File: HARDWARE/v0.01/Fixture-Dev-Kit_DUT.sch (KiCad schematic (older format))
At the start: 31 parts, among them J5? CHIP4LH, J6? CHIP4RH, J8? CHIP4B2B

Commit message: editing some files. cleaning stuff up.
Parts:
- J?: value JST -> BAT
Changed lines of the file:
@@
 P 900 6150
 F 0 "J?" H 900 6250 50  0000 C CNN
-F 1 "JST" H 900 5950 50  0000 C CNN
+F 1 "BAT" H 900 5950 50  0000 C CNN
 F 2 "" H 900 6150 50  0001 C CNN
 F 3 "" H 900 6150 50  0001 C CNN

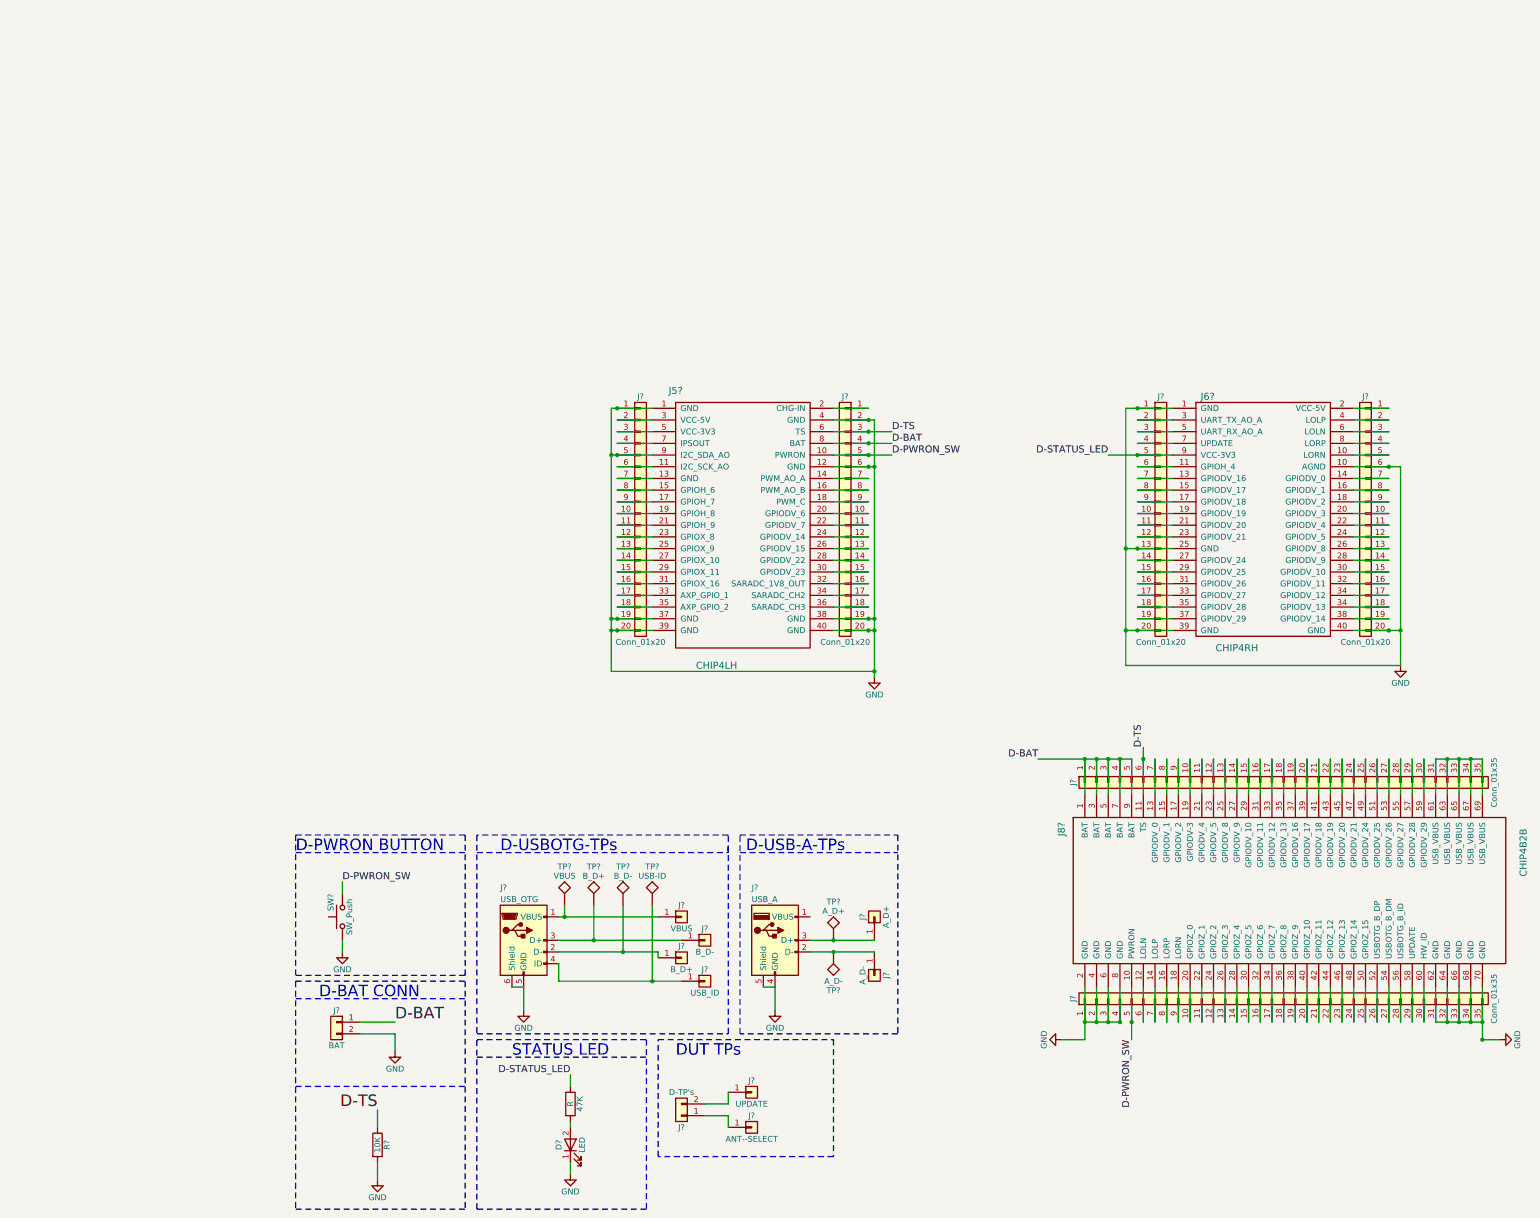
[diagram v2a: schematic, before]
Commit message: adding netlist and design rules check
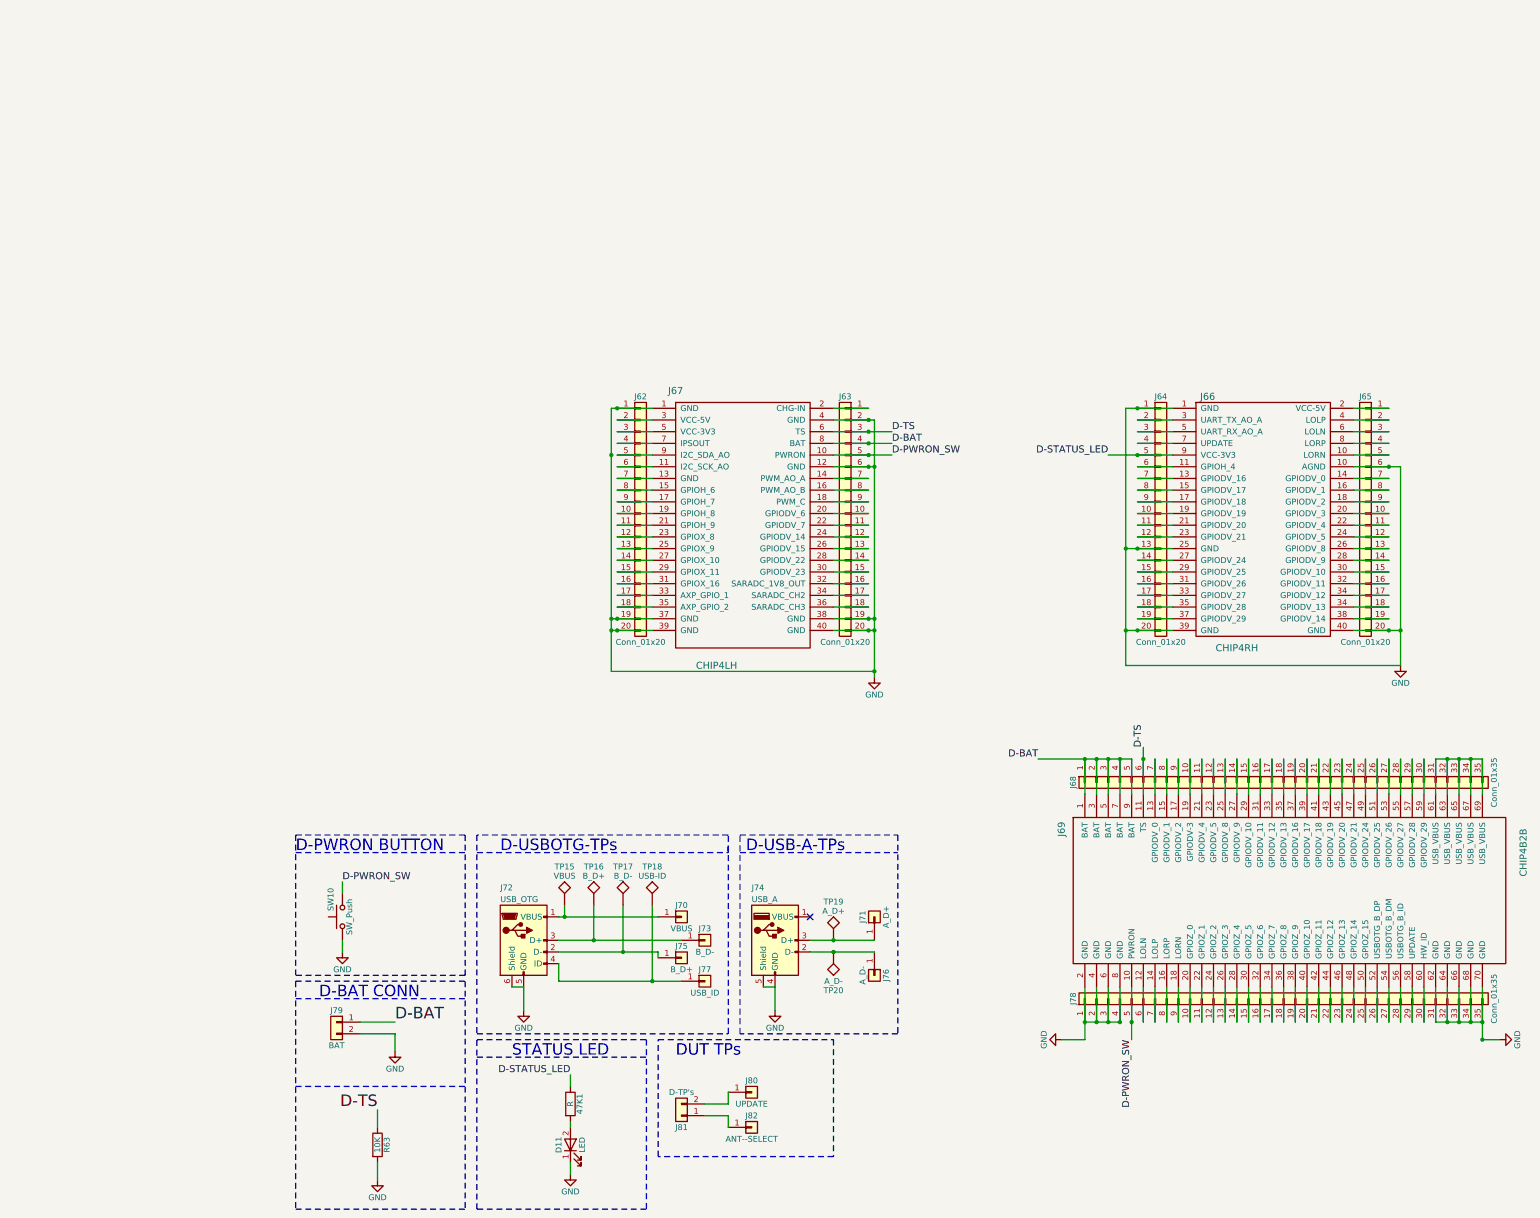
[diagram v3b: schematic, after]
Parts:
- gave numbers to parts that had none: 30
- renumbered 47K to 47K1
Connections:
- net GND: no longer J62.5 (Pin_5), J67.9 (I2C_SDA_AO)
- new net: J62.5 (Pin_5), J67.9 (I2C_SDA_AO)
- no-connect marks 0 -> 1
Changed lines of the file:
@@
 $EndDescr
 $Comp
-L Conn_01x20 J?
+L Conn_01x20 J65
 U 1 1 59EE26A0
 P 9700 1800
-F 0 "J?" H 9700 2800 50  0000 C CNN
+F 0 "J65" H 9700 2800 50  0000 C CNN
 F 1 "Conn_01x20" H 9700 700 50  0000 C CNN
 F 2 "" H 9700 1800 50  0001 C CNN
@@
 $EndComp
 $Comp
-L Conn_01x20 J?
+L Conn_01x20 J64
 U 1 1 59EE26E4
 P 7950 1800
-F 0 "J?" H 7950 2800 50  0000 C CNN
+F 0 "J64" H 7950 2800 50  0000 C CNN
 F 1 "Conn_01x20" H 7950 700 50  0000 C CNN
 F 2 "" H 7950 1800 50  0001 C CNN
@@
 $EndComp
 $Comp
-L Conn_01x20 J?
+L Conn_01x20 J63
 U 1 1 59EE2815
 P 5250 1800
-F 0 "J?" H 5250 2800 50  0000 C CNN
+F 0 "J63" H 5250 2800 50  0000 C CNN
 F 1 "Conn_01x20" H 5250 700 50  0000 C CNN
 F 2 "" H 5250 1800 50  0001 C CNN
@@
 $EndComp
 $Comp
-L Conn_01x20 J?
+L Conn_01x20 J62
 U 1 1 59EE289C
 P 3500 1800
-F 0 "J?" H 3500 2800 50  0000 C CNN
+F 0 "J62" H 3500 2800 50  0000 C CNN
 F 1 "Conn_01x20" H 3500 700 50  0000 C CNN
 F 2 "" H 3500 1800 50  0001 C CNN
@@
 	3600 1200 3300 1200
 Wire Wire Line
-	3250 1300 3600 1300
-Wire Wire Line
 	3600 1400 3300 1400
 Wire Wire Line
@@
 	5450 900  5150 900
 $Comp
-L GND #PWR?
+L GND #PWR059
 U 1 1 59EE39D0
 P 10000 3100
-F 0 "#PWR?" H 10000 2850 50  0001 C CNN
+F 0 "#PWR059" H 10000 2850 50  0001 C CNN
 F 1 "GND" H 10000 2950 50  0000 C CNN
 F 2 "" H 10000 3100 50  0001 C CNN
@@
 Connection ~ 7750 2800
 $Comp
-L GND #PWR?
+L GND #PWR060
 U 1 1 59EE3CBF
 P 5500 3200
-F 0 "#PWR?" H 5500 2950 50  0001 C CNN
+F 0 "#PWR060" H 5500 2950 50  0001 C CNN
 F 1 "GND" H 5500 3050 50  0000 C CNN
 F 2 "" H 5500 3200 50  0001 C CNN
@@
 Connection ~ 3300 2700
 Connection ~ 3250 1300
-Connection ~ 3300 1300
-$Comp
-L SW_Push SW?
+$Comp
+L SW_Push SW10
 U 1 1 59EE41F3
 P 950 5250
-F 0 "SW?" H 1000 5350 50  0000 L CNN
+F 0 "SW10" H 1000 5350 50  0000 L CNN
 F 1 "SW_Push" H 950 5190 50  0000 C CNN
 F 2 "" H 950 5450 50  0001 C CNN
@@
 D-PWRON_SW
 $Comp
-L GND #PWR?
+L GND #PWR061
 U 1 1 59EE44BA
 P 950 5550
-F 0 "#PWR?" H 950 5300 50  0001 C CNN
+F 0 "#PWR061" H 950 5300 50  0001 C CNN
 F 1 "GND" H 950 5400 50  0000 C CNN
 F 2 "" H 950 5550 50  0001 C CNN
@@
 D-BAT
 $Comp
-L Conn_01x02 J?
+L Conn_01x02 J79
 U 1 1 59EE490D
 P 900 6150
-F 0 "J?" H 900 6250 50  0000 C CNN
+F 0 "J79" H 900 6250 50  0000 C CNN
 F 1 "BAT" H 900 5950 50  0000 C CNN
 F 2 "" H 900 6150 50  0001 C CNN
@@
 $EndComp
 $Comp
-L GND #PWR?
+L GND #PWR062
 U 1 1 59EE4976
 P 1400 6400
-F 0 "#PWR?" H 1400 6150 50  0001 C CNN
+F 0 "#PWR062" H 1400 6150 50  0001 C CNN
 F 1 "GND" H 1400 6250 50  0000 C CNN
 F 2 "" H 1400 6400 50  0001 C CNN
@@
 D-BAT CONN\n
 $Comp
-L CHIP4B2B J8?
+L CHIP4B2B J69
 U 1 1 59EE53E4
 P 10800 5000
-F 0 "J8?" H 10300 8700 60  0000 C CNN
+F 0 "J69" H 10300 8700 60  0000 C CNN
 F 1 "CHIP4B2B" H 10500 4750 60  0000 C CNN
 F 2 "" H 10900 6550 60  0001 C CNN
@@
 $EndComp
 $Comp
-L Conn_01x35 J?
+L Conn_01x35 J78
 U 1 1 59EE5553
 P 9000 5950
-F 0 "J?" H 9000 7750 50  0000 C CNN
+F 0 "J78" H 9000 7750 50  0000 C CNN
 F 1 "Conn_01x35" H 9000 4150 50  0000 C CNN
 F 2 "" H 9000 5950 50  0001 C CNN
@@
 $EndComp
 $Comp
-L Conn_01x35 J?
+L Conn_01x35 J68
 U 1 1 59EE5A00
 P 9000 4100
-F 0 "J?" H 9000 5900 50  0000 C CNN
+F 0 "J68" H 9000 5900 50  0000 C CNN
 F 1 "Conn_01x35" H 9000 2300 50  0000 C CNN
 F 2 "" H 9000 4100 50  0001 C CNN
@@
 Connection ~ 10600 3900
 $Comp
-L GND #PWR?
+L GND #PWR063
 U 1 1 59EE8E82
 P 10850 6300
-F 0 "#PWR?" H 10850 6050 50  0001 C CNN
+F 0 "#PWR063" H 10850 6050 50  0001 C CNN
 F 1 "GND" H 10850 6150 50  0000 C CNN
 F 2 "" H 10850 6300 50  0001 C CNN
@@
 	10700 6300 10850 6300
 $Comp
-L GND #PWR?
+L GND #PWR064
 U 1 1 59EE9E75
 P 7100 6300
-F 0 "#PWR?" H 7100 6050 50  0001 C CNN
+F 0 "#PWR064" H 7100 6050 50  0001 C CNN
 F 1 "GND" H 7100 6150 50  0000 C CNN
 F 2 "" H 7100 6300 50  0001 C CNN
@@
 	1400 6250 1400 6400
 $Comp
-L GND #PWR?
+L GND #PWR065
 U 1 1 59EEAB1E
 P 1250 7500
-F 0 "#PWR?" H 1250 7250 50  0001 C CNN
+F 0 "#PWR065" H 1250 7250 50  0001 C CNN
 F 1 "GND" H 1250 7350 50  0000 C CNN
 F 2 "" H 1250 7500 50  0001 C CNN
@@
 $EndComp
 $Comp
-L R R?
+L R R63
 U 1 1 59EEAB48
 P 1250 7200
-F 0 "R?" V 1330 7200 50  0000 C CNN
+F 0 "R63" V 1330 7200 50  0000 C CNN
 F 1 "10K" V 1250 7200 50  0000 C CNN
 F 2 "" V 1180 7200 50  0001 C CNN
@@
 D-STATUS_LED
 $Comp
-L LED D?
+L LED D11
 U 1 1 59EEB9BD
 P 2900 7200
-F 0 "D?" H 2900 7300 50  0000 C CNN
+F 0 "D11" H 2900 7300 50  0000 C CNN
 F 1 "LED" H 2900 7100 50  0000 C CNN
 F 2 "" H 2900 7200 50  0001 C CNN
@@
 $EndComp
 $Comp
-L GND #PWR?
+L GND #PWR066
 U 1 1 59EEBA3C
 P 2900 7450
-F 0 "#PWR?" H 2900 7200 50  0001 C CNN
+F 0 "#PWR066" H 2900 7200 50  0001 C CNN
 F 1 "GND" H 2900 7300 50  0000 C CNN
 F 2 "" H 2900 7450 50  0001 C CNN
@@
 	2900 7450 2900 7350
 $Comp
-L R 47K
+L R 47K1
 U 1 1 59EEBC3E
 P 2900 6850
-F 0 "47K" V 2980 6850 50  0000 C CNN
+F 0 "47K1" V 2980 6850 50  0000 C CNN
 F 1 "R" V 2900 6850 50  0000 C CNN
 F 2 "" V 2830 6850 50  0001 C CNN
@@
 	2100 6450 3550 6450
 $Comp
-L CHIP4LH J5?
+L CHIP4LH J67
 U 1 1 59EF0A10
 P 4350 2950
-F 0 "J5?" H 3800 5150 60  0000 C CNN
+F 0 "J67" H 3800 5150 60  0000 C CNN
 F 1 "CHIP4LH" H 4150 2800 60  0000 C CNN
 F 2 "" H 4450 2950 60  0001 C CNN
@@
 $EndComp
 $Comp
-L CHIP4RH J6?
+L CHIP4RH J66
 U 1 1 59EF1105
 P 8850 2850
-F 0 "J6?" H 8350 4900 60  0000 C CNN
+F 0 "J66" H 8350 4900 60  0000 C CNN
 F 1 "CHIP4RH" H 8600 2750 60  0000 C CNN
 F 2 "" H 8900 2850 60  0001 C CNN
@@
 	7800 5850 7800 6150
 $Comp
-L USB_OTG J?
+L USB_OTG J72
 U 1 1 59EE3483
 P 2500 5450
-F 0 "J?" H 2300 5900 50  0000 L CNN
+F 0 "J72" H 2300 5900 50  0000 L CNN
 F 1 "USB_OTG" H 2300 5800 50  0000 L CNN
 F 2 "" H 2650 5400 50  0001 C CNN
@@
 $EndComp
 $Comp
-L Conn_01x01 J?
+L Conn_01x01 J70
 U 1 1 59EE3AA7
 P 3850 5250
-F 0 "J?" H 3850 5350 50  0000 C CNN
+F 0 "J70" H 3850 5350 50  0000 C CNN
 F 1 "VBUS" H 3850 5150 50  0000 C CNN
 F 2 "" H 3850 5250 50  0001 C CNN
@@
 $EndComp
 $Comp
-L Conn_01x01 J?
+L Conn_01x01 J73
 U 1 1 59EE3B2E
 P 4050 5450
-F 0 "J?" H 4050 5550 50  0000 C CNN
+F 0 "J73" H 4050 5550 50  0000 C CNN
 F 1 "B_D-" H 4050 5350 50  0000 C CNN
 F 2 "" H 4050 5450 50  0001 C CNN
@@
 $EndComp
 $Comp
-L Conn_01x01 J?
+L Conn_01x01 J75
 U 1 1 59EE3B75
 P 3850 5600
-F 0 "J?" H 3850 5700 50  0000 C CNN
+F 0 "J75" H 3850 5700 50  0000 C CNN
 F 1 "B_D+" H 3850 5500 50  0000 C CNN
 F 2 "" H 3850 5600 50  0001 C CNN
@@
 $EndComp
 $Comp
-L Conn_01x01 J?
+L Conn_01x01 J77
 U 1 1 59EE3BBF
 P 4050 5800
-F 0 "J?" H 4050 5900 50  0000 C CNN
+F 0 "J77" H 4050 5900 50  0000 C CNN
 F 1 "USB_ID" H 4050 5700 50  0000 C CNN
 F 2 "" H 4050 5800 50  0001 C CNN
@@
 $EndComp
 $Comp
-L TEST TP?
+L TEST TP15
 U 1 1 59EE3BFB
 P 2850 5150
-F 0 "TP?" H 2850 5450 50  0000 C BNN
+F 0 "TP15" H 2850 5450 50  0000 C BNN
 F 1 "VBUS" H 2850 5400 50  0000 C CNN
 F 2 "" H 2850 5150 50  0001 C CNN
@@
 $EndComp
 $Comp
-L TEST TP?
+L TEST TP16
 U 1 1 59EE3C66
 P 3100 5150
-F 0 "TP?" H 3100 5450 50  0000 C BNN
+F 0 "TP16" H 3100 5450 50  0000 C BNN
 F 1 "B_D+" H 3100 5400 50  0000 C CNN
 F 2 "" H 3100 5150 50  0001 C CNN
@@
 $EndComp
 $Comp
-L TEST TP?
+L TEST TP17
 U 1 1 59EE3CBB
 P 3350 5150
-F 0 "TP?" H 3350 5450 50  0000 C BNN
+F 0 "TP17" H 3350 5450 50  0000 C BNN
 F 1 "B_D-" H 3350 5400 50  0000 C CNN
 F 2 "" H 3350 5150 50  0001 C CNN
@@
 $EndComp
 $Comp
-L TEST TP?
+L TEST TP18
 U 1 1 59EE3D0F
 P 3600 5150
-F 0 "TP?" H 3600 5450 50  0000 C BNN
+F 0 "TP18" H 3600 5450 50  0000 C BNN
 F 1 "USB-ID" H 3600 5400 50  0000 C CNN
 F 2 "" H 3600 5150 50  0001 C CNN
@@
 	2800 5800 3850 5800
 $Comp
-L GND #PWR?
+L GND #PWR067
 U 1 1 59EE623C
 P 2500 6050
-F 0 "#PWR?" H 2500 5800 50  0001 C CNN
+F 0 "#PWR067" H 2500 5800 50  0001 C CNN
 F 1 "GND" H 2500 5900 50  0000 C CNN
 F 2 "" H 2500 6050 50  0001 C CNN
@@
 	4250 4700 4250 4650
 $Comp
-L USB_A J?
+L USB_A J74
 U 1 1 59EE80E3
 P 4650 5450
-F 0 "J?" H 4450 5900 50  0000 L CNN
+F 0 "J74" H 4450 5900 50  0000 L CNN
 F 1 "USB_A" H 4450 5800 50  0000 L CNN
 F 2 "" H 4800 5400 50  0001 C CNN
@@
 $EndComp
 $Comp
-L Conn_01x01 J?
+L Conn_01x01 J71
 U 1 1 59EE8606
 P 5500 5250
-F 0 "J?" H 5500 5350 50  0000 C CNN
+F 0 "J71" H 5500 5350 50  0000 C CNN
 F 1 "A_D+" H 5500 5150 50  0000 C CNN
 F 2 "" H 5500 5250 50  0001 C CNN
@@
 $EndComp
 $Comp
-L Conn_01x01 J?
+L Conn_01x01 J76
 U 1 1 59EE879F
 P 5500 5750
-F 0 "J?" H 5500 5850 50  0000 C CNN
+F 0 "J76" H 5500 5850 50  0000 C CNN
 F 1 "A_D-" H 5500 5650 50  0000 C CNN
 F 2 "" H 5500 5750 50  0001 C CNN
@@
 $EndComp
 $Comp
-L TEST TP?
+L TEST TP20
 U 1 1 59EE8980
 P 5150 5550
-F 0 "TP?" H 5150 5850 50  0000 C BNN
+F 0 "TP20" H 5150 5850 50  0000 C BNN
 F 1 "A_D-" H 5150 5800 50  0000 C CNN
 F 2 "" H 5150 5550 50  0001 C CNN
@@
 $EndComp
 $Comp
-L TEST TP?
+L TEST TP19
 U 1 1 59EE8A8A
 P 5150 5450
-F 0 "TP?" H 5150 5750 50  0000 C BNN
+F 0 "TP19" H 5150 5750 50  0000 C BNN
 F 1 "A_D+" H 5150 5700 50  0000 C CNN
 F 2 "" H 5150 5450 50  0001 C CNN
@@
 Connection ~ 5150 5550
 $Comp
-L GND #PWR?
+L GND #PWR068
 U 1 1 59EE91D1
 P 4650 6050
-F 0 "#PWR?" H 4650 5800 50  0001 C CNN
+F 0 "#PWR068" H 4650 5800 50  0001 C CNN
 F 1 "GND" H 4650 5900 50  0000 C CNN
 F 2 "" H 4650 6050 50  0001 C CNN
@@
 	4350 4700 5700 4700
 $Comp
-L Conn_01x01 J?
+L Conn_01x01 J80
 U 1 1 59EEA0FF
 P 4450 6750
-F 0 "J?" H 4450 6850 50  0000 C CNN
+F 0 "J80" H 4450 6850 50  0000 C CNN
 F 1 "UPDATE" H 4450 6650 50  0000 C CNN
 F 2 "" H 4450 6750 50  0001 C CNN
@@
 $EndComp
 $Comp
-L Conn_01x01 J?
+L Conn_01x01 J82
 U 1 1 59EEA2FD
 P 4450 7050
-F 0 "J?" H 4450 7150 50  0000 C CNN
+F 0 "J82" H 4450 7150 50  0000 C CNN
 F 1 "ANT--SELECT" H 4450 6950 50  0000 C CNN
 F 2 "" H 4450 7050 50  0001 C CNN
@@
 $EndComp
 $Comp
-L Conn_01x02 J?
+L Conn_01x02 J81
 U 1 1 59EEA72D
 P 3850 6950
-F 0 "J?" H 3850 7050 50  0000 C CNN
+F 0 "J81" H 3850 7050 50  0000 C CNN
 F 1 "D-TP's" H 3850 6750 50  0000 C CNN
 F 2 "" H 3850 6950 50  0001 C CNN
@@
 Wire Notes Line
 	3650 7300 3650 6300
+NoConn ~ 4950 5250
+Wire Wire Line
+	3600 1300 3300 1300
 $EndSCHEMATC

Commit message: updating a few blocks, adding test points
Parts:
- added J? (x2): VBUS, symbol Conn_01x01
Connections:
- net at J70.1 (Pin_1), J72.1 (VBUS), TP15.1: now also J?.1 (Pin_1)
- net at J74.1 (VBUS): now also J?.1 (Pin_1)
- no-connect marks 1 -> 0
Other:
- note added: "DUT"
- note added: "TO DO:\n- is PWRON and BAT break out necessary if headers \nare already broken out?"
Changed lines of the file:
@@
 Wire Notes Line
 	3650 7300 3650 6300
-NoConn ~ 4950 5250
 Wire Wire Line
 	3600 1300 3300 1300
+Text Notes 550  800  0    197  ~ 0
+DUT
+$Comp
+L Conn_01x01 J?
+U 1 1 59F0C6A2
+P 3200 6050
+F 0 "J?" H 3200 6150 50  0000 C CNN
+F 1 "VBUS" H 3200 5950 50  0000 C CNN
+F 2 "" H 3200 6050 50  0001 C CNN
+F 3 "" H 3200 6050 50  0001 C CNN
+	1    3200 6050
+	1    0    0    -1
+$EndComp
+Wire Wire Line
+	3000 6050 3000 5250
+Connection ~ 3000 5250
+$Comp
+L Conn_01x01 J?
+U 1 1 59F0CD26
+P 5150 4900
+F 0 "J?" H 5150 5000 50  0000 C CNN
+F 1 "VBUS" H 5150 4800 50  0000 C CNN
+F 2 "" H 5150 4900 50  0001 C CNN
+F 3 "" H 5150 4900 50  0001 C CNN
+	1    5150 4900
+	1    0    0    -1
+$EndComp
+Wire Wire Line
+	4950 4900 4950 5250
+Text Notes -1900 -1550 0    197  ~ 0
+TO DO:\n- is PWRON and BAT break out necessary if headers \nare already broken out?
 $EndSCHEMATC
